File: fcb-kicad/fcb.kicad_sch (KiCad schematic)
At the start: 22 parts, among them U1 TPS5430DDA, U2 AMS1117-3.3, U3 DL-RTS4432, U4 LSM6DS3, U5 STM32F411CEUx

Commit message: kicad into folder :)
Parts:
- added H1, H2, H3, H4: MountingHole, MountingHole:MountingHole_3.2mm_M3, symbol Mechanical:MountingHole
- added J?: Conn_01x08_Male, symbol Connector:Conn_01x08_Male
- gave numbers to parts that had none: 4

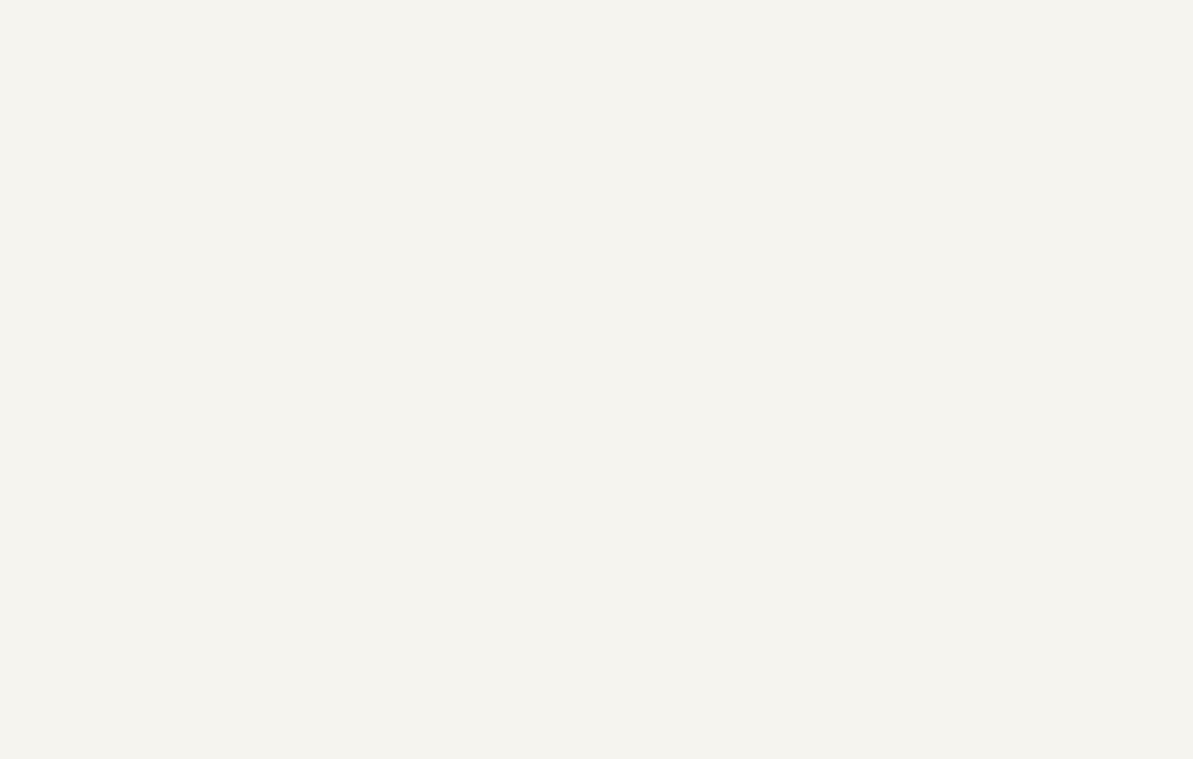
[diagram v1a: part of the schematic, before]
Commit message: Added BMP388 symbol
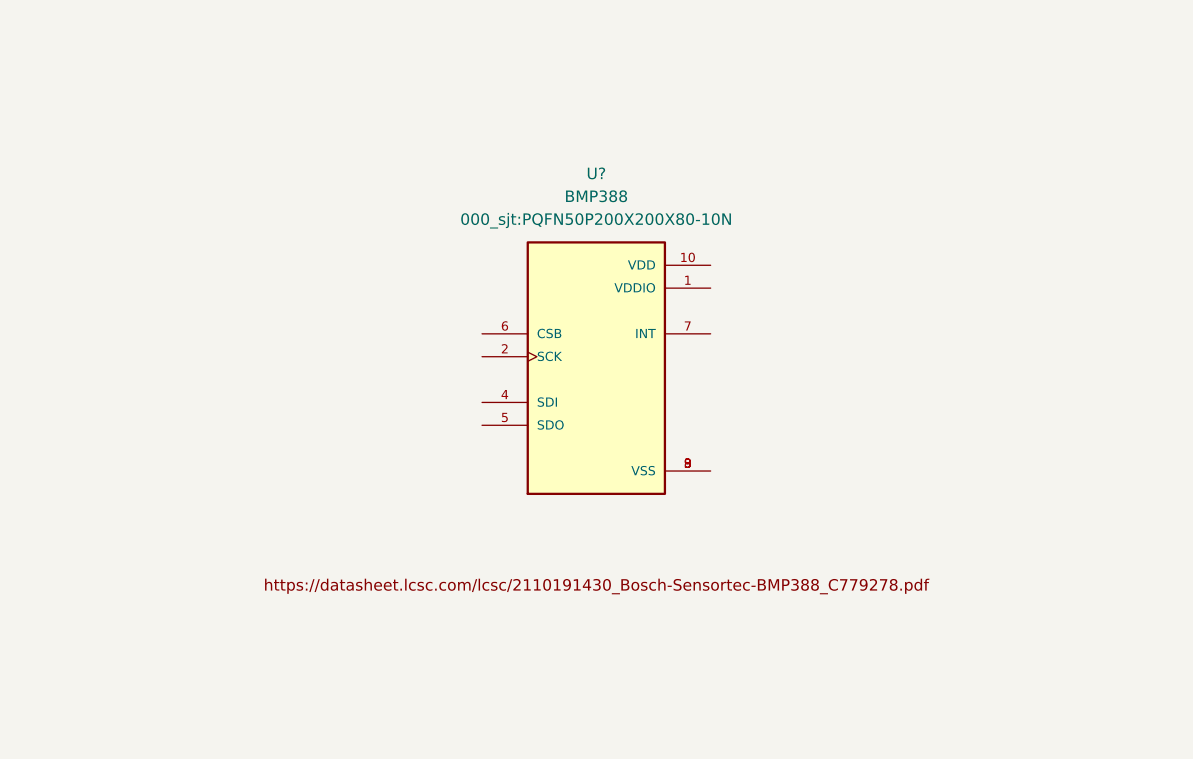
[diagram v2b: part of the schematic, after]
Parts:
- added U?: BMP388, 000_sjt:PQFN50P200X200X80-10N, symbol 000_sjt:BMP388
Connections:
- new net: U?.3 (VSS), U?.8 (VSS), U?.9 (VSS)
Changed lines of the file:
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@@
     (pin "3")
+  )
+  (symbol (lib_id "000_sjt:BMP388") (at 120.65 102.87 0) (unit 1)
+    (in_bom yes) (on_board yes) (fields_autoplaced)
+    (property "Reference" "U?" (id 0) (at 120.65 80.01 0))
+    (property "Value" "BMP388" (id 1) (at 120.65 82.55 0))
+    (property "Footprint" "000_sjt:PQFN50P200X200X80-10N" (id 2) (at 120.65 85.09 0))
+    (property "Datasheet" "" (id 3) (at 120.65 102.87 0)
+      (effects (font (size 1.27 1.27)) (justify left bottom) hide)
+    )
+    (property "PARTREV" "1.1" (id 4) (at 120.65 102.87 0)
+      (effects (font (size 1.27 1.27)) (justify left bottom) hide)
+    )
+    (property "MANUFACTURER" "BOSCH" (id 5) (at 120.65 102.87 0)
+      (effects (font (size 1.27 1.27)) (justify left bottom) hide)
+    )
+    (property "STANDARD" "IPC 7351B" (id 6) (at 120.65 102.87 0)
+      (effects (font (size 1.27 1.27)) (justify left bottom) hide)
+    )
+    (pin "1")
+    (pin "10")
+    (pin "2")
+    (pin "3")
+    (pin "4")
+    (pin "5")
+    (pin "6")
+    (pin "7")
+    (pin "8")
+    (pin "9")
   )
   (symbol (lib_id "power:GND") (at 282.575 62.23 0) (unit 1)
@@
       (reference "U6") (unit 1) (value "W25Q128JVS") (footprint "Package_SO:SOIC-8_5.23x5.23mm_P1.27mm")
     )
-  )
+    (path "/6cbc87ce-e9b3-4fa4-ba2f-289ef0e94ca6"
+      (reference "U?") (unit 1) (value "BMP388") (footprint "000_sjt:PQFN50P200X200X80-10N")
+    )
+  )

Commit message: cpu pins
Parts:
- removed U?: BMP388, 000_sjt:PQFN50P200X200X80-10N, symbol 000_sjt:BMP388
- added C?: 4u7, symbol Device:C_Small
- added CL1, CL2: 8p, symbol Device:C_Small
- added R? (x3): 10k, Resistor_SMD:R_0603_1608Metric, symbol Device:R_Small
- added Rext: 1k, symbol Device:R_Small
- added SW?: SW_Push, symbol Switch:SW_Push
- added SW?: SW_SPDT, symbol Switch:SW_SPDT
- added Y1: 16 MHz, symbol Device:Crystal_GND24
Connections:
- net +3V3: now also U5.1 (VBAT), U5.24 (VDD), U5.36 (VDD), U5.48 (VDD), R?.1, R?.1
- net -BATT: now also U5.23 (VSS), U5.35 (VSS), U5.47 (VSS), U5.49 (VSS), U5.8 (VSSA), C?.1, CL1.2, CL2.1, R?.2, SW?.1, Y1.2, Y1.4
- net AI_VBAT: now reaches U5.10 (PA0)
- net AI_CRNT: now reaches U5.11 (PA1)
- net AI_5V_1: now reaches U5.12 (PA2)
- net AI_5V_2: now reaches U5.13 (PA3)
- net AI_3V: now reaches U5.14 (PA4)
- net SPI1_SCK: now reaches U5.15 (PA5)
- net SPI1_MISO: now reaches U5.16 (PA6)
- net SPI1_MOSI: now reaches U5.17 (PA7)
- net TIM3_CH3: now reaches U5.18 (PB0)
- net TIM3_CH4: now reaches U5.19 (PB1)
- net RAD_IRQ_N: now reaches U5.2 (PC13)
- net RAD_IRQ_N: now also U3.14 (nIRQ)
- net IMU_CS: now reaches U5.20 (PB2)
- net SPI2_SCK: now reaches U5.21 (PB10)
- net at U5.22 (VCAP1): now also C?.2
- net IMU_INT1: now reaches U5.25 (PB12)
- net GPIO_PB13: now reaches U5.26 (PB13)
- net SPI2_MISO: now reaches U5.27 (PB14)
- net SPI2_MOSI: now reaches U5.28 (PB15)
- net FLASH_CS_N: now reaches U5.29 (PA8)
- net RAD_CS_N: now reaches U5.3 (PC14)
- net RAD_CS_N: now also U3.13 (nSEL)
- net USART1_TX: now reaches U5.30 (PA9)
- net USART1_RX: now reaches U5.31 (PA10)
- net USB_DM: now reaches U5.32 (PA11)
- net USB_DP: now reaches U5.33 (PA12)
- net SWDIO: now reaches U5.34 (PA13)
- net SWCLK: now reaches U5.37 (PA14)
- net GPIO_PA15: now reaches U5.38 (PA15)
- net SWO: now reaches U5.39 (PB3)
- net RAD_GPIO_0: now reaches U5.4 (PC15)
- net RAD_GPIO_0: now also U3.6 (GPIO_0)
- net TIM3_CH1: now reaches U5.40 (PB4)
- net TIM3_CH2: now reaches U5.41 (PB5)
- net I2C1_SCL: now reaches U5.42 (PB6)
- net I2C1_SDA: now reaches U5.43 (PB7)
- net CPU_BOOT0: now reaches U5.44 (BOOT0)
- net CPU_BOOT0: now also SW?.2 (B)
- net GPIO_PB8: now reaches U5.45 (PB8)
- net GPIO_PB9: now reaches U5.46 (PB9)
- net OSC_IN: now reaches U5.5 (PH0)
- net OSC_IN: now also CL1.1, Y1.3
- net OSC_OUT: now reaches U5.6 (PH1)
- net OSC_OUT: now also Rext.2
- net CPU_NRST: now reaches U5.7 (NRST)
- net CPU_NRST: now also R?.2, SW?.2
- net +3.3VA: now reaches U5.9 (VDDA)
- new net: CL2.2, Rext.1, Y1.1
- new net: R?.1, SW?.1 (A)
- new net: R?.2, SW?.3 (C)
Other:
- added sheet I2C Peripherials (i2c.kicad_sch)
- added sheet SPI peripherials (spi.kicad_sch)
- note added: "16MHZ --> 96 MHz HCLK"
- note added: "3V3 LINEAR REGULATOR"
- note added: "5V BUCK REGULATOR"
- note added: "CL1 = CL2 = C C = 2 * (CL_osc - C_stray) CL_osc = 9pF (datasheet) C_stray = 5 pF --> 2 * (9p - 5p) = 8p Rext = 1/(2*pi*Fosc*C) ≈ 1240 Ω --> 1k"
- note added: "MCU BOOT & RESET"
- note added: "OSCILLATOR"
- note removed: "BUCK REGULATOR"
- note removed: "LINEAR REGULATOR"
- moved on the sheet: C1, C2, C3, C4, C5, D1, H1, H2, H3, H4, L1, R1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

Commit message: hierarchic schemas, paljon muuta kivaa
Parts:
- removed BZ1: MLT-8530, Buzzer_Beeper:Buzzer_TDK_PS1240P02BT_D12.2mm_H6.5mm, symbol Device:Buzzer
- removed D2: 1N4148W, Diode_SMD:D_SOD-123, symbol Device:D_Small
- removed J?: Conn_01x08_Male, symbol Connector:Conn_01x08_Male
- removed Q1: S8050 J3Y, Package_TO_SOT_SMD:SOT-23, symbol Device:Q_NPN_BEC
- removed R4: 470, Resistor_SMD:R_0603_1608Metric, symbol Device:R_Small
- removed U3: DL-RTS4432, 000_sjt:DL-RTS4432_board, symbol 000_sjt:DL-RTS4432
- removed U4: LSM6DS3, Package_LGA:LGA-14_3x2.5mm_P0.5mm_LayoutBorder3x4y, symbol Sensor_Motion:LSM6DS3
- removed U6: W25Q128JVS, Package_SO:SOIC-8_5.23x5.23mm_P1.27mm, symbol Memory_Flash:W25Q128JVS
- added C11: 4u7, Capacitor_SMD:C_0603_1608Metric, symbol Device:C_Small
- added C12, C13, C14, C15: 100n, Capacitor_SMD:C_0603_1608Metric, symbol Device:C_Small
- added C16: 1u, symbol Device:C_Small
- added C17: 10n, symbol Device:C_Small
- added D2, D?: LED_red, LED_SMD:LED_0603_1608Metric, symbol Device:LED
- added D4: B5819W SL, Diode_SMD:D_SOD-123, symbol Device:D_Schottky
- added FB1, FB2, FB3: 500mA 600Ω@100M, Capacitor_SMD:C_0805_2012Metric, symbol Device:FerriteBead_Small
- added J1: Conn_01x08_Male, symbol Connector:Conn_01x08_Male
- added J2: SWD, symbol Connector_Generic:Conn_02x05_Odd_Even
- added R13, R14, R15, R16: 22R, symbol Device:R
- added R? (x2): 1k, symbol Device:R_Small
- C1: value 10u -> 10u 50V; footprint Capacitor_SMD:C_1206_3216Metric_Pad1.33x1.80mm_HandSolder -> Capacitor_SMD:C_1206_3216Metric
- C2: value 100n -> 100n 50V; footprint Capacitor_SMD:C_0603_1608Metric_Pad1.08x0.95mm_HandSolder -> Capacitor_SMD:C_0603_1608Metric
- C5: footprint Capacitor_SMD:C_0603_1608Metric_Pad1.08x0.95mm_HandSolder -> Capacitor_SMD:C_0603_1608Metric
- C6, C7: footprint Capacitor_SMD:C_1206_3216Metric_Pad1.33x1.80mm_HandSolder -> Capacitor_SMD:C_0603_1608Metric
- C8: renamed from C?; footprint (none) -> Capacitor_SMD:C_0603_1608Metric
- gave numbers to parts that had none: 5
- renumbered Rext to Rext1
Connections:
- net GPIO_PA15 is gone; now on net BUZZER: U5.38 (PA15)
- net +3.3VA: now also C16.1, C17.1, FB3.2
- net +3V3: now also C11.2, C12.2, C13.2, C14.2, C15.2, D?.2 (A), FB3.1, J2.1 (Pin_1)
- net +5V: now also D2.2 (A), D4.1 (K)
- net +BATT: now also FB1.1, J1.8 (Pin_8); no longer C1.2, C2.2, U1.7 (VIN)
- net AI_CRNT: now also J1.7 (Pin_7)
- net CPU_NRST: now also R16.2
- net SWCLK: now also R14.2
- net SWDIO: now also R13.2
- net SWO: now also R15.2
- net TIM3_CH1: now also J1.4 (Pin_4)
- net TIM3_CH2: now also J1.3 (Pin_3)
- net TIM3_CH3: now also J1.2 (Pin_2)
- net TIM3_CH4: now also J1.1 (Pin_1)
- net -BATT renamed GND
- net GND: now also C11.1, C12.1, C13.1, C14.1, C15.1, FB2.1, J1.6 (Pin_6), J2.3 (Pin_3), J2.5 (Pin_5), J2.9 (Pin_9), R?.2, R?.2; no longer U5.8 (VSSA)
- new net: C1.2, C2.2, FB1.2, U1.7 (VIN)
- new net: D2.1 (K), R?.1
- new net: J2.10 (Pin_10), R16.1
- new net: J2.2 (Pin_2), R13.1
- new net: J2.4 (Pin_4), R14.1
- new net: J2.6 (Pin_6), R15.1
- new net: D?.1 (K), R?.1
- new net 5V_USB: D4.2 (A)
- new net GNDA: C16.2, C17.2, FB2.2, U5.8 (VSSA)
- no-connect marks 1 -> 4
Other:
- added sheet IO (io.kicad_sch)
- note added: ""GND" = Battery negative terminal"
- note added: "1A rated"
- note added: "3V3 Linear regulator"
- note added: "Analog inputs, GPIO, Buzzer, User LEDs, USB, UART"
- note added: "Barometer, Magnetometer, I2c connector"
- note added: "Decoupling"
- note added: "ESC 4IN1 connector"
- note added: "IMU, Radio module, Flash memory"
- note added: "JST-SH 8-pin male Pinout to fit Racestar Rev35 35A ESC"
- note added: "MCU boot & reset"
- note added: "Oscillator"
- note added: "Power status LEDs"
- note added: "Programming / debug header"
- note added: "SHEETS"
- note added: "STM32F411CEU6"
- note added: "Take power from USB if 5V not connected"
- note added: "Vbatt -> 5V Buck regulator"
- note added: "bulk 10u + 100n per VDD / VBAT pin"
- note removed: "1A RATED"
- note removed: "3V3 LINEAR REGULATOR"
- note removed: "5V BUCK REGULATOR"
- note removed: "BUZZER CIRCUIT"
- note removed: "MCU BOOT & RESET"
- note removed: "OSCILLATOR"
- company: (none) -> University of Oulu
- title: (none) -> Connectors, Power, MCU
- moved on the sheet: C1, C2, C3, C4, C5, C6, C7, C8, CL1, CL2, D1, H1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

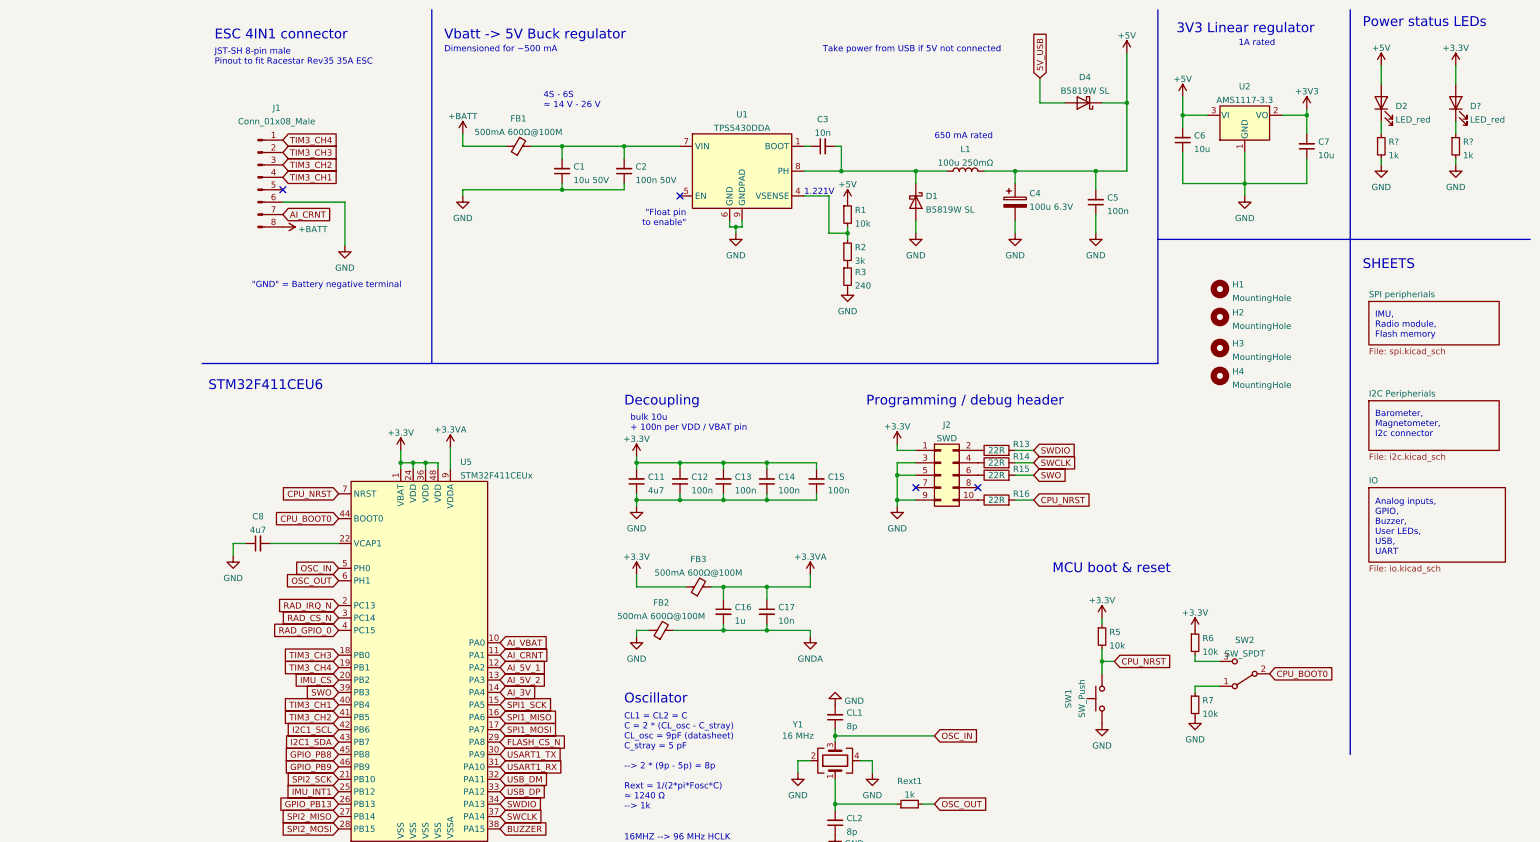
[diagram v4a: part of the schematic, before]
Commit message: 4in1 connector library part, SPI CS pullups, migrate magnetometer cirtuit
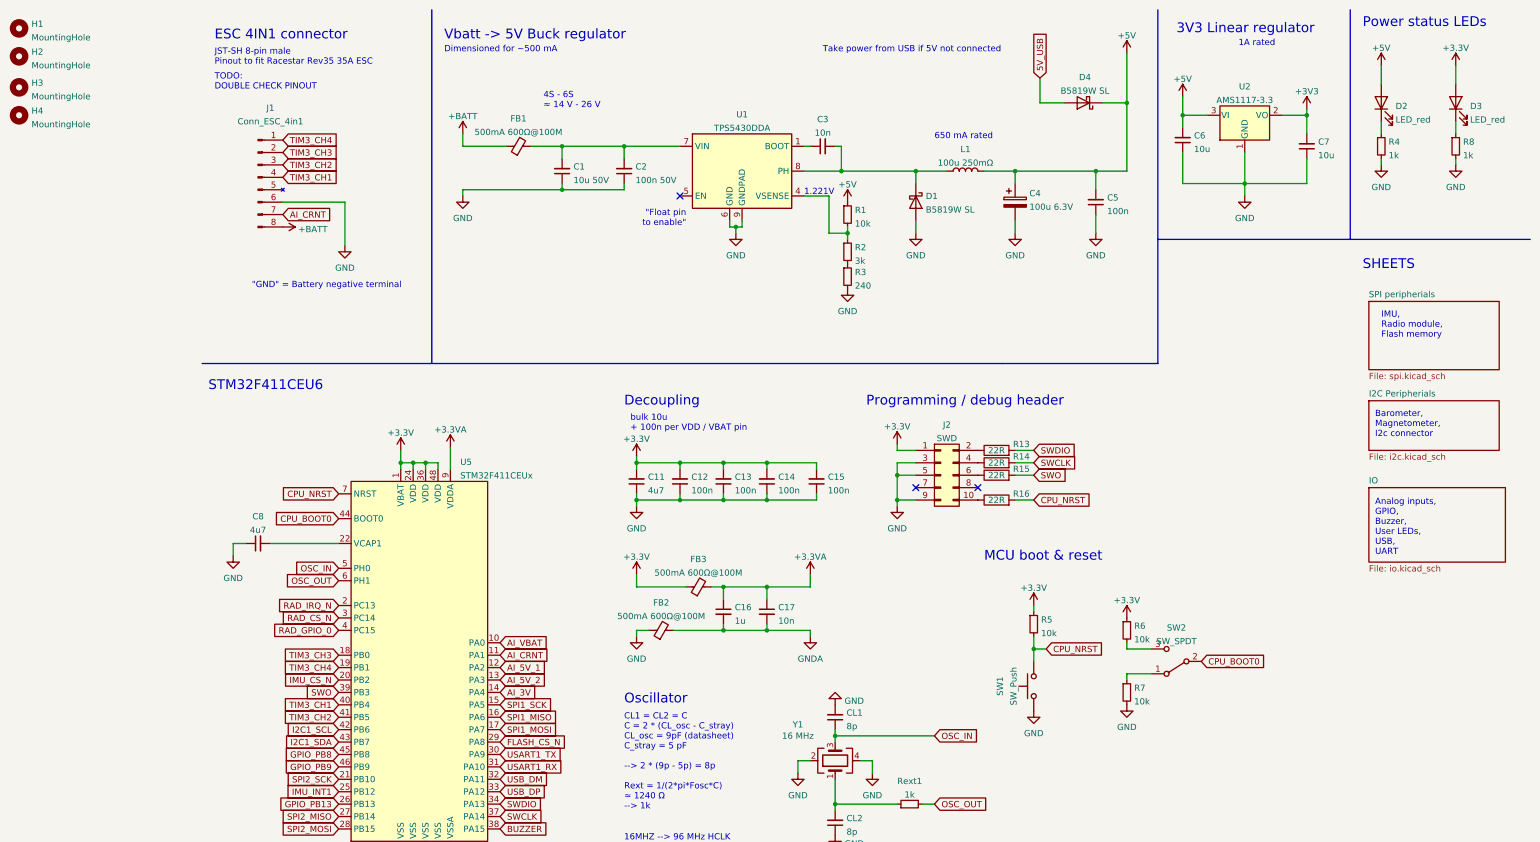
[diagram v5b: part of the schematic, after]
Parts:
- removed J1: Conn_01x08_Male, symbol Connector:Conn_01x08_Male
- added J1: Conn_ESC_4in1, symbol 000_sjt:Conn_ESC_4in1
- gave numbers to parts that had none: 3
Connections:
- net +BATT: now also J1.8 (VBAT)
- net AI_CRNT: now also J1.7 (CRNT)
- net GND: now also J1.6 (GND)
- net TIM3_CH1: now also J1.4 (IN1)
- net TIM3_CH2: now also J1.3 (IN2)
- net TIM3_CH3: now also J1.2 (IN3)
- net TIM3_CH4: now also J1.1 (IN4)
- net IMU_CS renamed IMU_CS_N
- no-connect marks 4 -> 3
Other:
- note added: "TODO: DOUBLE CHECK PINOUT"
- moved on the sheet: H1, H2, H3, H4, R5, R6, R7, SW1, SW2
